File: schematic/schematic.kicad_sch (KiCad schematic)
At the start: 32 parts, among them IC2 AS312, J3 USB_C_Receptacle_USB2.0, SW2 SW_Push, SW3 SW_Push, U1 ESP32-S3-WROOM-1, U3 AM2302

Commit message: more Routing
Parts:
- added +5V: 5v, TestPoint:TestPoint_Loop_D2.50mm_Drill1.85mm, symbol Connector:TestPoint
- added GND1: GND, TestPoint:TestPoint_Loop_D2.50mm_Drill1.85mm, symbol Connector:TestPoint
- renumbered SW3 to BOOT1, SW2 to RESET1, Switch+ to Switch+1, Switch- to Switch-1
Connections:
- net +5V: now also +5V.1
- net GND: now also GND1.1
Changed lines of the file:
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@@
 	)
 	(junction
+		(at 168.91 32.385)
+		(diameter 0)
+		(color 0 0 0 0)
+	)
+	(junction
 		(at 46.355 41.91)
 		(diameter 0)
@@
 	)
 	(junction
+		(at 169.545 21.59)
+		(diameter 0)
+		(color 0 0 0 0)
+	)
+	(junction
 		(at 54.61 36.83)
 		(diameter 0)
@@
 	(wire
 		(pts
+			(xy 168.91 21.59) (xy 169.545 21.59)
+		)
+		(stroke
+			(width 0)
+			(type default)
+		)
+	)
+	(wire
+		(pts
 			(xy 107.95 30.48) (xy 107.95 43.815)
 		)
@@
 	(wire
 		(pts
+			(xy 168.91 32.385) (xy 168.91 34.29)
+		)
+		(stroke
+			(width 0)
+			(type default)
+		)
+	)
+	(wire
+		(pts
 			(xy 88.9 29.845) (xy 88.9 27.94)
 		)
@@
 	(wire
 		(pts
-			(xy 168.91 21.59) (xy 169.545 21.59)
-		)
-		(stroke
-			(width 0)
-			(type default)
-		)
-	)
-	(wire
-		(pts
 			(xy 139.7 30.48) (xy 139.7 32.385)
 		)
@@
 	(wire
 		(pts
+			(xy 181.61 34.29) (xy 168.91 34.29)
+		)
+		(stroke
+			(width 0)
+			(type default)
+		)
+	)
+	(wire
+		(pts
 			(xy 292.1 95.25) (xy 288.29 95.25)
 		)
@@
 	(wire
 		(pts
+			(xy 169.545 21.59) (xy 182.88 21.59)
+		)
+		(stroke
+			(width 0)
+			(type default)
+		)
+	)
+	(wire
+		(pts
 			(xy 237.49 105.41) (xy 227.33 105.41)
 		)
@@
 	)
 	(symbol
+		(lib_id "Connector:TestPoint")
+		(at 181.61 34.29 270)
+		(unit 1)
+		(exclude_from_sim no)
+		(in_bom yes)
+		(on_board yes)
+		(dnp no)
+		(property "Reference" "GND1"
+			(at 186.182 36.83 0)
+			(effects
+				(font
+					(size 1.27 1.27)
+				)
+				(justify left)
+			)
+		)
+		(property "Value" "GND"
+			(at 183.642 36.83 0)
+			(effects
+				(font
+					(size 1.27 1.27)
+				)
+				(justify left)
+			)
+		)
+		(property "Footprint" "TestPoint:TestPoint_Loop_D2.50mm_Drill1.85mm"
+			(at 181.61 39.37 0)
+			(effects
+				(font
+					(size 1.27 1.27)
+				)
+				(hide yes)
+			)
+		)
+		(property "Datasheet" "~"
+			(at 181.61 39.37 0)
+			(effects
+				(font
+					(size 1.27 1.27)
+				)
+				(hide yes)
+			)
+		)
+		(property "Description" ""
+			(at 181.61 34.29 0)
+			(effects
+				(font
+					(size 1.27 1.27)
+				)
+				(hide yes)
+			)
+		)
+		(pin "1"
+		)
+		(instances
+			(project "schematic"
+				(path "/374f5031-bd65-4a4b-92ce-befdd0c9f08b"
+					(reference "GND1")
+					(unit 1)
+				)
+			)
+		)
+	)
+	(symbol
 		(lib_id "AS312:AS312")
 		(at 247.65 105.41 0)
@@
 		(dnp no)
 		(fields_autoplaced yes)
-		(property "Reference" "SW2"
+		(property "Reference" "RESET1"
 			(at 27.94 88.9 0)
 			(effects
@@
 			(project "schematic"
 				(path "/374f5031-bd65-4a4b-92ce-befdd0c9f08b"
-					(reference "SW2")
+					(reference "RESET1")
 					(unit 1)
 				)
@@
 	)
 	(symbol
+		(lib_id "Connector:TestPoint")
+		(at 182.88 21.59 270)
+		(unit 1)
+		(exclude_from_sim no)
+		(in_bom yes)
+		(on_board yes)
+		(dnp no)
+		(property "Reference" "+5V"
+			(at 187.452 24.13 0)
+			(effects
+				(font
+					(size 1.27 1.27)
+				)
+				(justify left)
+			)
+		)
+		(property "Value" "5v"
+			(at 184.912 24.13 0)
+			(effects
+				(font
+					(size 1.27 1.27)
+				)
+				(justify left)
+			)
+		)
+		(property "Footprint" "TestPoint:TestPoint_Loop_D2.50mm_Drill1.85mm"
+			(at 182.88 26.67 0)
+			(effects
+				(font
+					(size 1.27 1.27)
+				)
+				(hide yes)
+			)
+		)
+		(property "Datasheet" "~"
+			(at 182.88 26.67 0)
+			(effects
+				(font
+					(size 1.27 1.27)
+				)
+				(hide yes)
+			)
+		)
+		(property "Description" ""
+			(at 182.88 21.59 0)
+			(effects
+				(font
+					(size 1.27 1.27)
+				)
+				(hide yes)
+			)
+		)
+		(pin "1"
+		)
+		(instances
+			(project "schematic"
+				(path "/374f5031-bd65-4a4b-92ce-befdd0c9f08b"
+					(reference "+5V")
+					(unit 1)
+				)
+			)
+		)
+	)
+	(symbol
 		(lib_id "Device:C_Small")
 		(at 250.19 54.61 90)
@@
 		(dnp no)
 		(fields_autoplaced yes)
-		(property "Reference" "SW3"
+		(property "Reference" "BOOT1"
 			(at 31.115 127.635 0)
 			(effects
@@
 			(project "schematic"
 				(path "/374f5031-bd65-4a4b-92ce-befdd0c9f08b"
-					(reference "SW3")
+					(reference "BOOT1")
 					(unit 1)
 				)
@@
 		(on_board yes)
 		(dnp no)
-		(property "Reference" "Switch-"
+		(property "Reference" "Switch-1"
 			(at 271.78 147.828 0)
 			(effects
@@
 			(project "schematic"
 				(path "/374f5031-bd65-4a4b-92ce-befdd0c9f08b"
-					(reference "Switch-")
+					(reference "Switch-1")
 					(unit 1)
 				)
@@
 		(on_board yes)
 		(dnp no)
-		(property "Reference" "Switch+"
+		(property "Reference" "Switch+1"
 			(at 256.54 149.098 0)
 			(effects
@@
 			(project "schematic"
 				(path "/374f5031-bd65-4a4b-92ce-befdd0c9f08b"
-					(reference "Switch+")
+					(reference "Switch+1")
 					(unit 1)
 				)

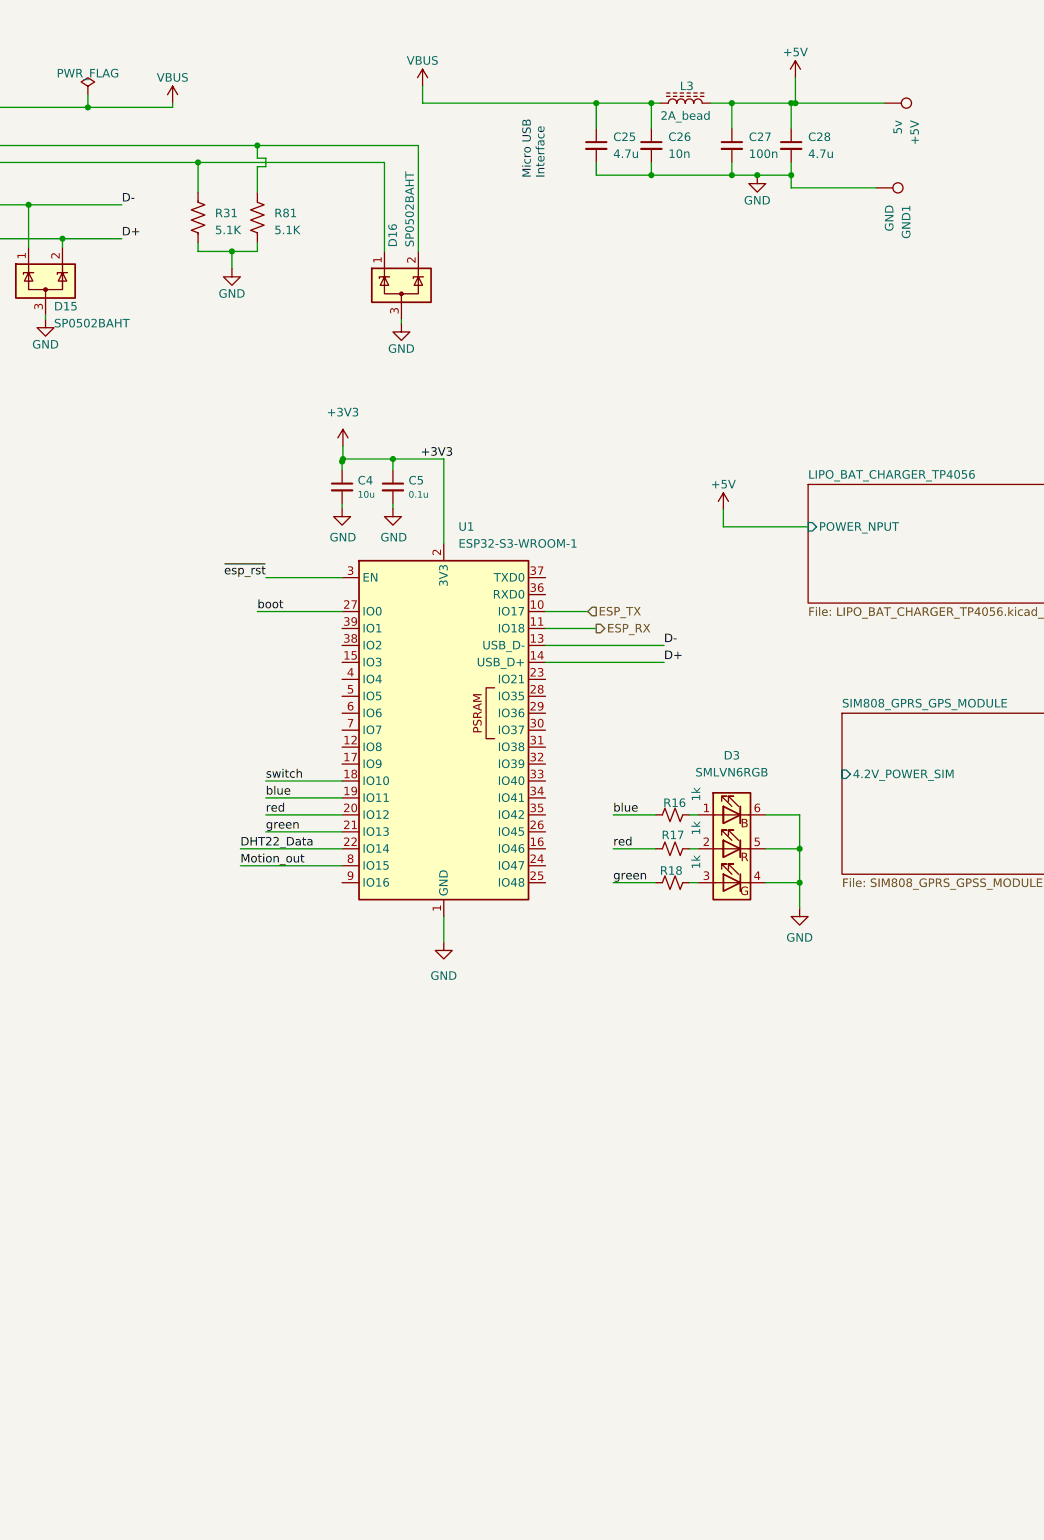
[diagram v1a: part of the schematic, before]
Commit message: changinge mcu and shift level
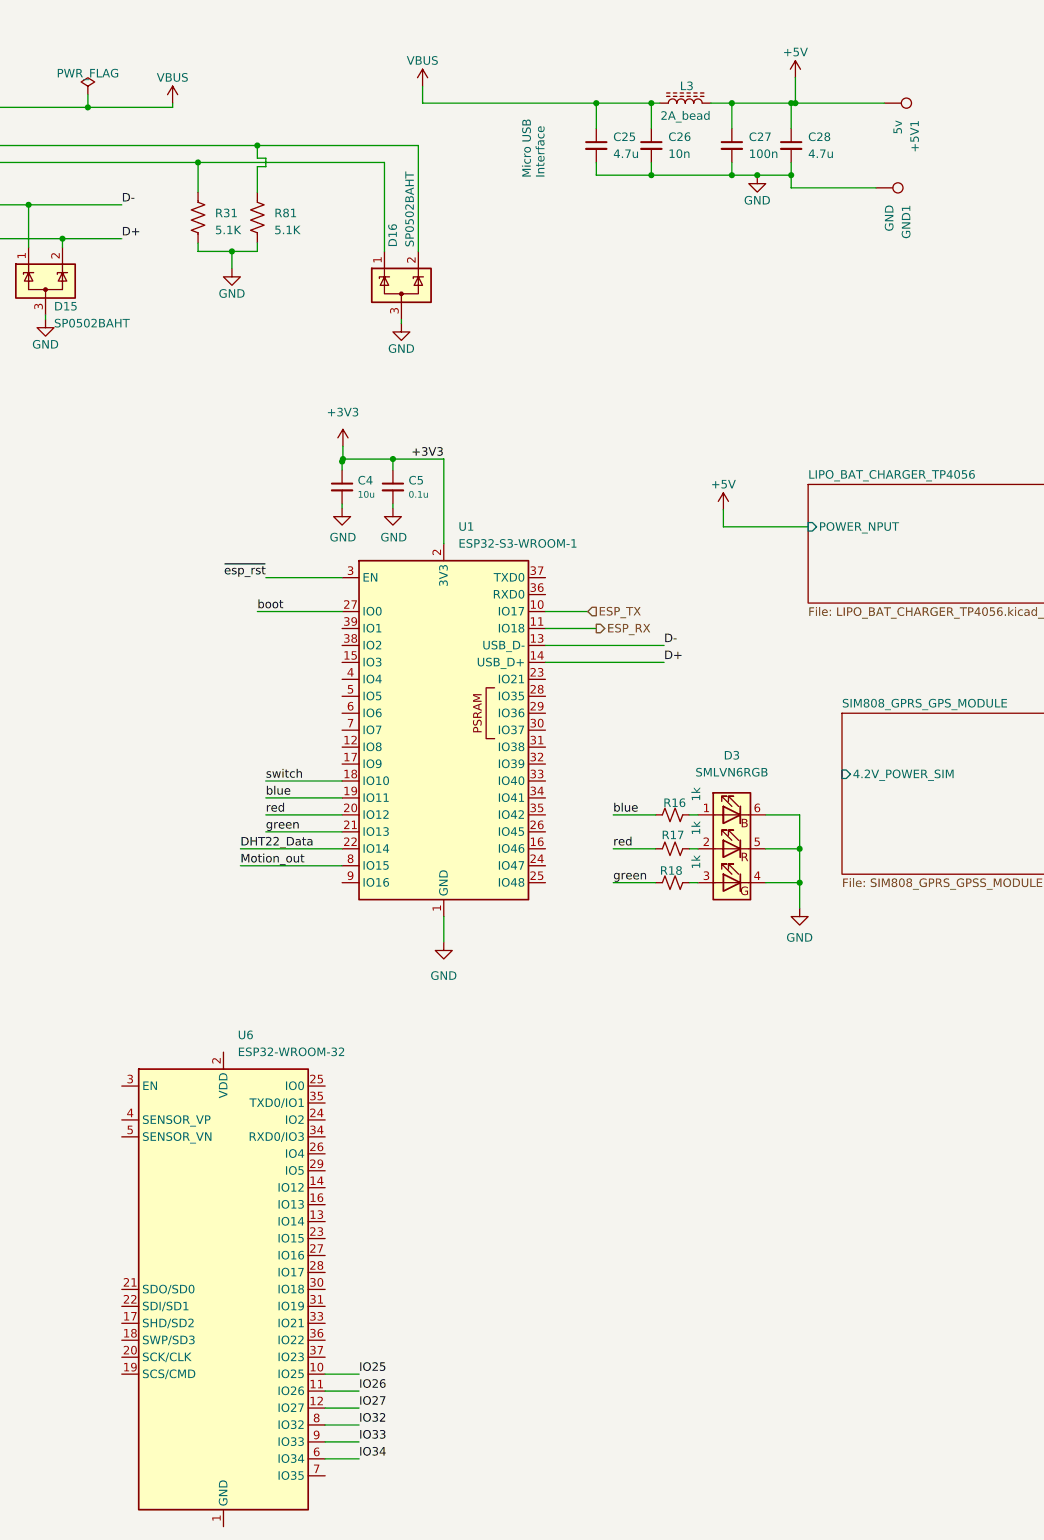
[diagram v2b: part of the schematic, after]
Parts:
- added U6: ESP32-WROOM-32, RF_Module:ESP32-WROOM-32, symbol RF_Module:ESP32-WROOM-32
- renumbered +5V to +5V1
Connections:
- new net: U6.1 (GND), U6.15 (GND), U6.38 (GND), U6.39 (GND)
- new net IO25: U6.10 (IO25)
- new net IO26: U6.11 (IO26)
- new net IO27: U6.12 (IO27)
- new net IO32: U6.8 (IO32)
- new net IO33: U6.9 (IO33)
- new net IO34: U6.6 (IO34)

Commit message: changinge mcu and shift level
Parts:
- removed C4: 10u, Capacitor_SMD:C_0402_1005Metric, symbol Device:C_Small
- removed C5: 0.1u, Capacitor_SMD:C_0402_1005Metric, symbol Device:C_Small
- removed U1: ESP32-S3-WROOM-1, RF_Module:ESP32-S3-WROOM-1, symbol RF_Module:ESP32-S3-WROOM-1
- added C10: 10u, Capacitor_SMD:C_0402_1005Metric, symbol Device:C_Small
- added C11: 0.1u, Capacitor_SMD:C_0402_1005Metric, symbol Device:C_Small
- added C13: 22uF, Capacitor_SMD:C_0402_1005Metric, symbol Device:C_Small
- added C14: 100nF, Capacitor_SMD:C_0402_1005Metric, symbol Device:C_Small
- added C15, C16: 22pF, Capacitor_SMD:C_0402_1005Metric, symbol Device:C_Small
- added D10, D11, D12: B5819W, Diode_SMD:D_SOD-123, symbol Device:D_Schottky_Small
- added D13: BAT54C, Package_TO_SOT_SMD:SOT-23, symbol Diode:BAT54C
- added D9: D_Schottky_Small, Diode_SMD:D_SOD-123, symbol Device:D_Schottky_Small
- added Q10, Q11: MMBT3904, Package_TO_SOT_SMD:SOT-23, symbol Transistor_BJT:MMBT3904
- added R11, R19, R20, R21: 10k, Resistor_SMD:R_0402_1005Metric, symbol Device:R_Small_US
- added R22: 220R, Resistor_SMD:R_0402_1005Metric, symbol Device:R_Small_US
- added U8: CH340T(SSOP20W), Package_SO:SSOP-20_5.3x7.2mm_P0.65mm, symbol GCL_Integrated-Circuits:CH340T(SSOP20W)
- added Y1: 12MHz, Crystal:Crystal_SMD_2520-4Pin_2.5x2.0mm, symbol Device:Crystal_GND2_Small
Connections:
- net +3V3: now also U6.2 (VDD), C10.1, C11.1
- net +5V: now also C13.1, D9.1 (K), R11.1, U8.19 (VCC)
- net D+: now also U8.6 (UD+)
- net D-: now also U8.7 (UD-)
- net DHT22_Data: now also U6.31 (IO19)
- net ESP_RX: now also U6.34 (RXD0/IO3), D10.2 (A), R19.2
- net ESP_TX: now also U6.35 (TXD0/IO1), D11.1 (K)
- net GND: now also U6.1 (GND), U6.15 (GND), U6.38 (GND), U6.39 (GND), C10.2, C11.2, C13.2, C14.2, C15.2, C16.2, U8.8 (GND), Y1.2
- net Motion_out: now also U6.36 (IO22)
- net blue: now also U6.23 (IO15)
- net boot: now also U6.25 (IO0), D13.2
- net green: now also U6.16 (IO13)
- net red: now also U6.14 (IO12)
- net switch: now also U6.33 (IO21)
- net ~{esp_rst}: now also U6.3 (EN), D12.2 (A)
- net IO2: now reaches U6.24 (IO2)
- net IO2: now also D13.1
- net IO4: now reaches U6.26 (IO4)
- new net: C16.1, U8.10 (XO), Y1.3
- new net: D10.1 (K), U8.3 (TXD)
- new net: D11.2 (A), R11.2, U8.4 (RXD)
- new net: C14.1, R19.1, U8.5 (V3)
- new net: C15.1, U8.9 (XI), Y1.1
- new net: Q10.1 (B), R20.1
- new net: D12.1 (K), Q10.3 (C)
- new net: D13.3, R22.1
- new net: Q11.3 (C), R22.2
- new net: Q11.1 (B), R21.1
- new net dtr: Q10.2 (E), Q11.2 (E), R20.2, R21.2, U8.15 (DTR#), U8.16 (RTS#)
- no-connect marks 2 -> 8
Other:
- note added: "0"
- note added: "1"
- note added: "Auto Reset Circuit"
- note added: "Auto program"
- note added: "DTR RTS->EN IO0"
- moved on the sheet: U6

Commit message: MORE Routing with Global names
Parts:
- removed D9: D_Schottky_Small, Diode_SMD:D_SOD-123, symbol Device:D_Schottky_Small
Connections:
- no-connect marks 8 -> 20
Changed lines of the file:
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@@
 	)
 	(no_connect
+		(at -77.47 170.18)
+	)
+	(no_connect
+		(at -46.99 162.56)
+	)
+	(no_connect
 		(at -200.025 78.74)
 	)
 	(no_connect
+		(at -77.47 172.72)
+	)
+	(no_connect
 		(at -200.025 71.12)
 	)
 	(no_connect
+		(at -77.47 162.56)
+	)
+	(no_connect
+		(at -46.99 152.4)
+	)
+	(no_connect
+		(at -46.99 190.5)
+	)
+	(no_connect
+		(at -46.99 144.78)
+	)
+	(no_connect
 		(at -200.025 73.66)
 	)
 	(no_connect
+		(at -46.99 157.48)
+	)
+	(no_connect
 		(at -200.025 76.2)
 	)
 	(no_connect
+		(at -46.99 160.02)
+	)
+	(no_connect
 		(at 43.18 50.8)
 	)
@@
 	)
 	(no_connect
+		(at -46.99 172.72)
+	)
+	(no_connect
 		(at 43.18 53.34)
 	)
@@
 		(at -200.025 66.04)
 	)
+	(no_connect
+		(at -77.47 175.26)
+	)
+	(no_connect
+		(at -77.47 165.1)
+	)
 	(wire
 		(pts
@@
 	(wire
 		(pts
-			(xy -46.99 180.34) (xy -41.91 180.34)
+			(xy -46.99 180.34) (xy -35.56 180.34)
 		)
 		(stroke
@@
 	(wire
 		(pts
-			(xy -46.99 175.26) (xy -41.91 175.26)
+			(xy -46.99 175.26) (xy -35.56 175.26)
 		)
 		(stroke
@@
 	(wire
 		(pts
-			(xy -46.99 185.42) (xy -41.91 185.42)
+			(xy -46.99 185.42) (xy -35.56 185.42)
 		)
 		(stroke
@@
 	(wire
 		(pts
-			(xy -46.99 187.96) (xy -41.91 187.96)
+			(xy -46.99 187.96) (xy -35.56 187.96)
 		)
 		(stroke
@@
 	(wire
 		(pts
-			(xy -245.11 42.545) (xy -236.855 42.545)
-		)
-		(stroke
-			(width 0)
-			(type default)
-		)
-	)
-	(wire
-		(pts
 			(xy 76.2 21.59) (xy 76.2 22.225)
 		)
@@
 	(wire
 		(pts
-			(xy -46.99 182.88) (xy -41.91 182.88)
+			(xy -46.99 182.88) (xy -35.56 182.88)
 		)
 		(stroke
@@
 	(wire
 		(pts
-			(xy -46.99 177.8) (xy -41.91 177.8)
+			(xy -46.99 177.8) (xy -35.56 177.8)
 		)
 		(stroke
@@
 		)
 	)
+	(global_label "IO25"
+		(shape input)
+		(at -35.56 175.26 0)
+		(fields_autoplaced yes)
+		(effects
+			(font
+				(size 1.27 1.27)
+			)
+			(justify left)
+		)
+		(property "Intersheetrefs" "${INTERSHEET_REFS}"
+			(at -28.2205 175.26 0)
+			(effects
+				(font
+					(size 1.27 1.27)
+				)
+				(justify left)
+				(hide yes)
+			)
+		)
+	)
+	(global_label "IO34"
+		(shape input)
+		(at -35.56 187.96 0)
+		(fields_autoplaced yes)
+		(effects
+			(font
+				(size 1.27 1.27)
+			)
+			(justify left)
+		)
+		(property "Intersheetrefs" "${INTERSHEET_REFS}"
+			(at -28.2205 187.96 0)
+			(effects
+				(font
+					(size 1.27 1.27)
+				)
+				(justify left)
+				(hide yes)
+			)
+		)
+	)
 	(global_label "IO4"
 		(shape input)
@@
 		)
 	)
+	(global_label "IO33"
+		(shape input)
+		(at -35.56 185.42 0)
+		(fields_autoplaced yes)
+		(effects
+			(font
+				(size 1.27 1.27)
+			)
+			(justify left)
+		)
+		(property "Intersheetrefs" "${INTERSHEET_REFS}"
+			(at -28.2205 185.42 0)
+			(effects
+				(font
+					(size 1.27 1.27)
+				)
+				(justify left)
+				(hide yes)
+			)
+		)
+	)
 	(global_label "ESP_TX"
 		(shape input)
@@
 		)
 	)
+	(global_label "IO26"
+		(shape input)
+		(at -35.56 177.8 0)
+		(fields_autoplaced yes)
+		(effects
+			(font
+				(size 1.27 1.27)
+			)
+			(justify left)
+		)
+		(property "Intersheetrefs" "${INTERSHEET_REFS}"
+			(at -28.2205 177.8 0)
+			(effects
+				(font
+					(size 1.27 1.27)
+				)
+				(justify left)
+				(hide yes)
+			)
+		)
+	)
+	(global_label "IO27"
+		(shape input)
+		(at -35.56 180.34 0)
+		(fields_autoplaced yes)
+		(effects
+			(font
+				(size 1.27 1.27)
+			)
+			(justify left)
+		)
+		(property "Intersheetrefs" "${INTERSHEET_REFS}"
+			(at -28.2205 180.34 0)
+			(effects
+				(font
+					(size 1.27 1.27)
+				)
+				(justify left)
+				(hide yes)
+			)
+		)
+	)
+	(global_label "IO32"
+		(shape input)
+		(at -35.56 182.88 0)
+		(fields_autoplaced yes)
+		(effects
+			(font
+				(size 1.27 1.27)
+			)
+			(justify left)
+		)
+		(property "Intersheetrefs" "${INTERSHEET_REFS}"
+			(at -28.2205 182.88 0)
+			(effects
+				(font
+					(size 1.27 1.27)
+				)
+				(justify left)
+				(hide yes)
+			)
+		)
+	)
 	(global_label "ESP_RX"
 		(shape input)
@@
 					(unit 1)
 				)
-			)
-		)
-	)
-	(symbol
-		(lib_id "Device:D_Schottky_Small")
-		(at -247.65 42.545 180)
-		(unit 1)
-		(exclude_from_sim no)
-		(in_bom yes)
-		(on_board yes)
-		(dnp no)
-		(property "Reference" "D9"
-			(at -247.65 40.005 0)
-			(effects
-				(font
-					(size 1.27 1.27)
-				)
-			)
-		)
-		(property "Value" "D_Schottky_Small"
-			(at -247.396 39.37 0)
-			(effects
-				(font
-					(size 1.27 1.27)
-				)
-				(hide yes)
-			)
-		)
-		(property "Footprint" "Diode_SMD:D_SOD-123"
-			(at -247.65 42.545 90)
-			(effects
-				(font
-					(size 1.27 1.27)
-				)
-				(hide yes)
-			)
-		)
-		(property "Datasheet" "~"
-			(at -247.65 42.545 90)
-			(effects
-				(font
-					(size 1.27 1.27)
-				)
-				(hide yes)
-			)
-		)
-		(property "Description" ""
-			(at -247.65 42.545 0)
-			(effects
-				(font
-					(size 1.27 1.27)
-				)
-				(hide yes)
-			)
-		)
-		(pin "1"
-		)
-		(pin "2"
-		)
-		(instances
-			(project "schematic"
-				(path "/374f5031-bd65-4a4b-92ce-befdd0c9f08b"
-					(reference "D9")
-					(unit 1)
-				)
